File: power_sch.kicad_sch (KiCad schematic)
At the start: 18 parts, among them Q6 RUM002N05T2L, Q7 RUM002N05T2L, U3 TPS7A2601DRVR, U4 TPS7A2601DRVR

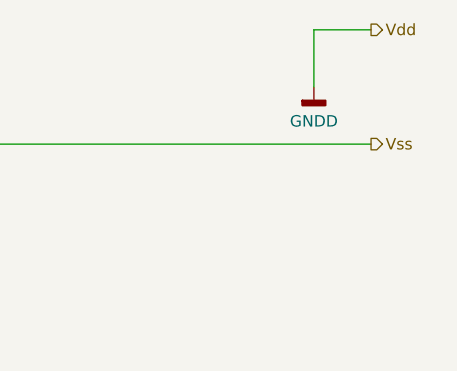
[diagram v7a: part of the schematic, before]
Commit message: Fix wrong wiring, add pcb design.
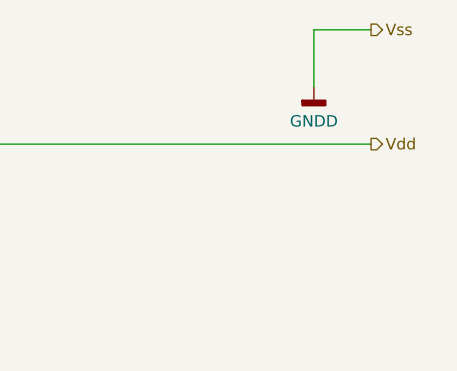
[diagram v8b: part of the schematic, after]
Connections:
- net Vss renamed Vdd
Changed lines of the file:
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@@
 		)
 	)
-	(hierarchical_label "Vss"
+	(hierarchical_label "Vdd"
 		(shape output)
 		(at 266.7 44.45 0)
@@
 		)
 	)
-	(hierarchical_label "Vdd"
+	(hierarchical_label "Vss"
 		(shape output)
 		(at 266.7 31.75 0)
